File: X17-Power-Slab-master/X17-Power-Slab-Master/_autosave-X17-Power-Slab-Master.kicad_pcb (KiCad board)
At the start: 2 copper layers, 302.3 x 119 mm, 61 parts, among them J2 ET60T-D04-3-08-D04-X-R1-S, J3 796636-6, J4 Conn_01x05, Q2 TSM340N06CP ROG, SW2 1825910-6, U1 AZ1117IH-3.3TRG1, U4 STM32F091CCTx, U7 ABLS-8.000MHZ-B2-T

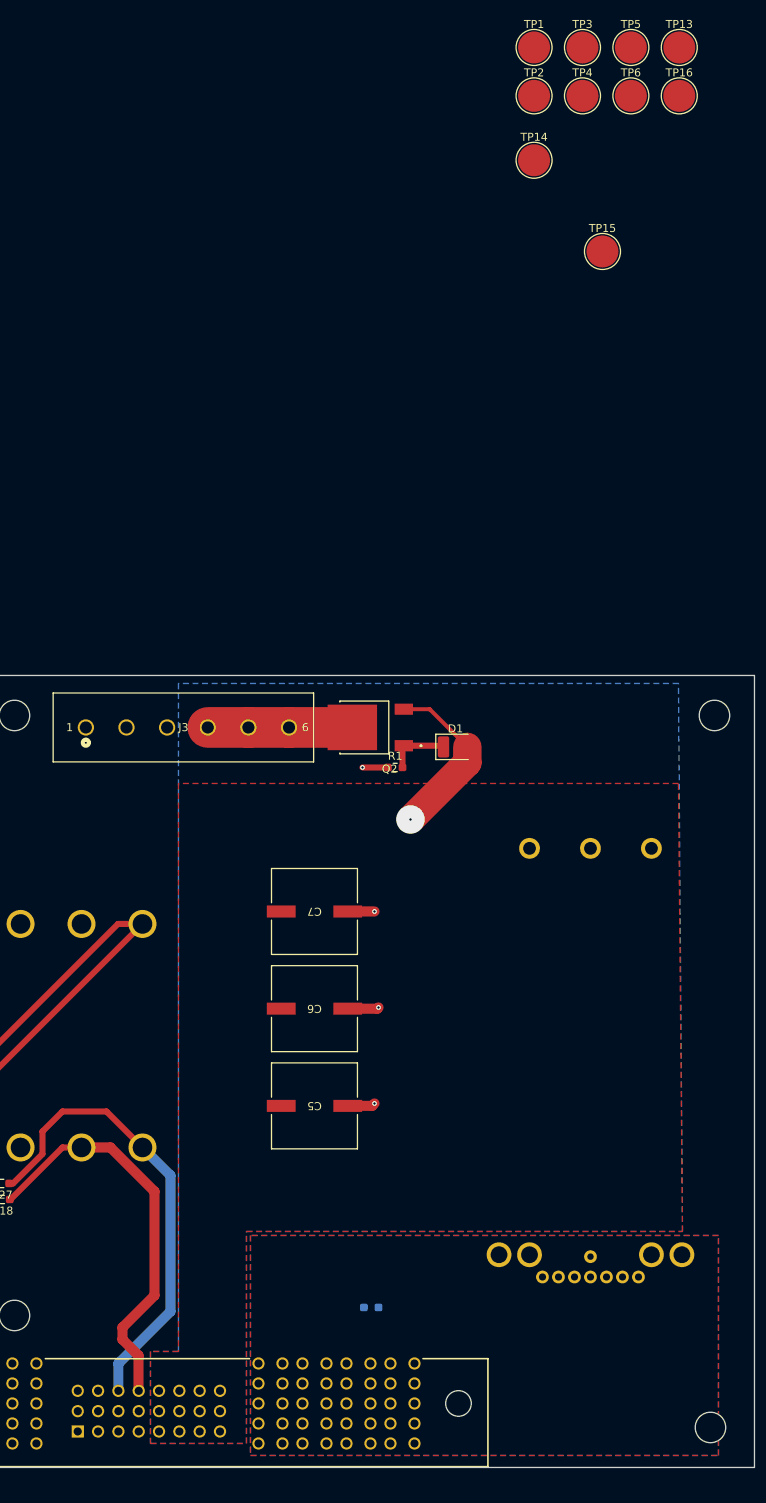
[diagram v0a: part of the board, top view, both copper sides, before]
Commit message: More connections
Fixing errors and thermal relief
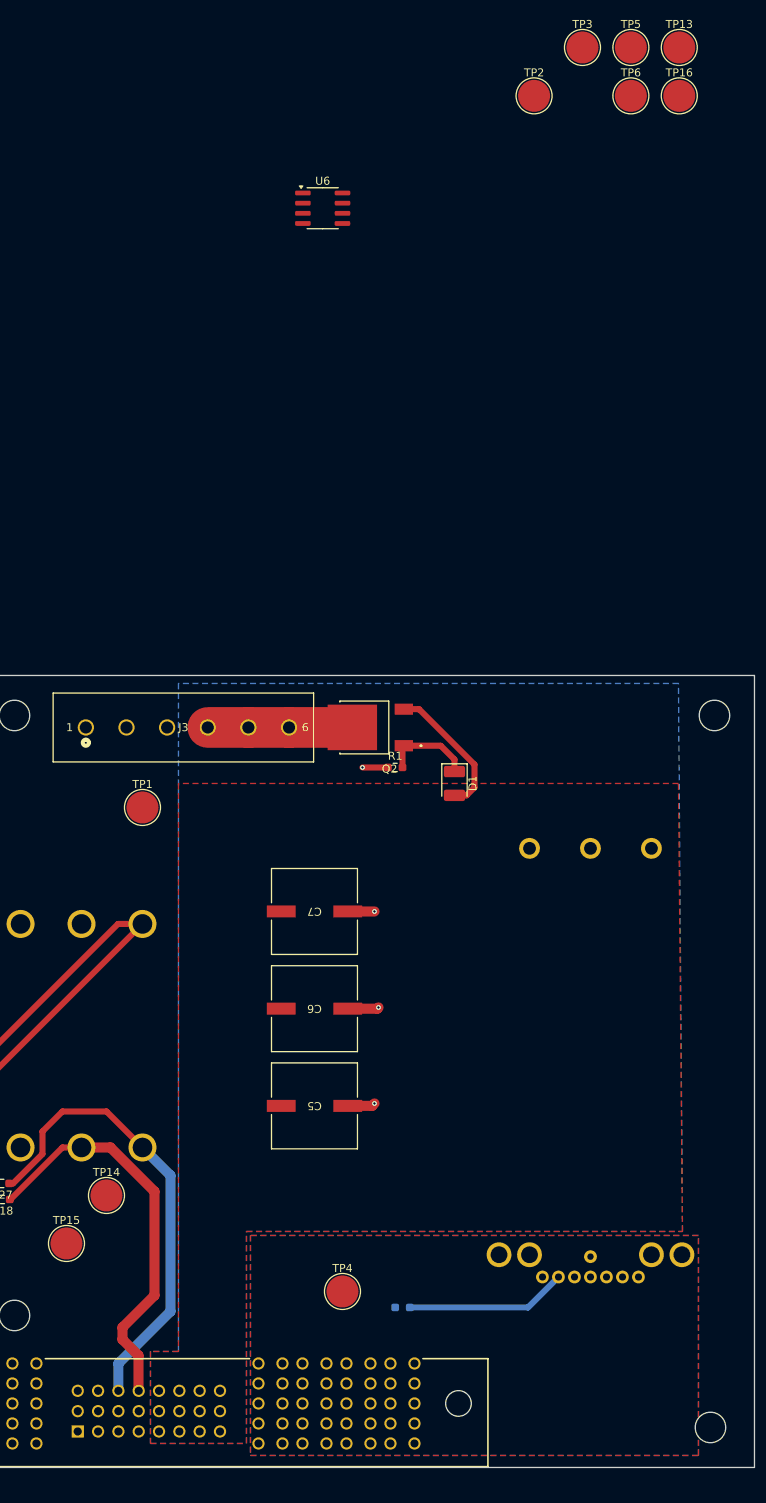
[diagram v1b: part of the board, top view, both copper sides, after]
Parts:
- added U6: MAX485E, Package_SO:SOIC-8_3.9x4.9mm_P1.27mm, F.Cu at (115.0, -14.9)
- moved TP4 152.4 mm to (117.5, 120.5)
- moved TP15 140.9 mm to (83.0, 114.5)
- moved TP14 140.0 mm to (88.0, 108.5)
- moved TP1 106.9 mm to (92.5, 60.0)
- moved D1 4.57 mm to (131.5, 57.0), turned to -90 degrees
- moved R10 3.91 mm to (125.0, 122.5)
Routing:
- net Net-(U8-SA0/SA1): track 0.00 -> 20.2 mm
- net 48V_GND: track 21.9 -> 17.5 mm, vias 1 -> 0
- net Net-(D1-K): track 8.23 -> 11.3 mm
